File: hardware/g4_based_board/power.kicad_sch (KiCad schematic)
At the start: 13 parts, among them U1 tps2117, U6 AZ1117-3.3

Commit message: auto updated
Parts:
- renumbered C18 to C50, C19 to C51, C22 to C52, D2 to D22, JP20 to JP61, R25 to R70, R77 to R71, R78 to R72, TP4 to TP30, TP5 to TP31, TP6 to TP32, U1 to U6, U6 to U7
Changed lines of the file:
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@@
 		(dnp no)
 		(fields_autoplaced yes)
-		(property "Reference" "#PWR042"
+		(property "Reference" "#PWR0243"
 			(at 192.532 137.922 0)
 			(effects
@@
 			(project "data_logger"
 				(path "/9bc93932-ff5f-4f35-96cf-dfa5f042acb6/ab250e5c-6a0e-43ed-b42b-bd03a881d896"
-					(reference "#PWR042")
+					(reference "#PWR0243")
 					(unit 1)
 				)
@@
 		(dnp no)
 		(fields_autoplaced yes)
-		(property "Reference" "TP6"
+		(property "Reference" "TP32"
 			(at 229.87 124.968 0)
 			(effects
@@
 			(project "data_logger"
 				(path "/9bc93932-ff5f-4f35-96cf-dfa5f042acb6/ab250e5c-6a0e-43ed-b42b-bd03a881d896"
-					(reference "TP6")
+					(reference "TP32")
 					(unit 1)
 				)
@@
 		(dnp no)
 		(fields_autoplaced yes)
-		(property "Reference" "#PWR014"
+		(property "Reference" "#PWR0234"
 			(at 132.08 121.92 0)
 			(effects
@@
 			(project "data_logger"
 				(path "/9bc93932-ff5f-4f35-96cf-dfa5f042acb6/ab250e5c-6a0e-43ed-b42b-bd03a881d896"
-					(reference "#PWR014")
+					(reference "#PWR0234")
 					(unit 1)
 				)
@@
 		(dnp no)
 		(fields_autoplaced yes)
-		(property "Reference" "R25"
+		(property "Reference" "R70"
 			(at 157.226 87.1219 0)
 			(effects
@@
 			(project "data_logger"
 				(path "/9bc93932-ff5f-4f35-96cf-dfa5f042acb6/ab250e5c-6a0e-43ed-b42b-bd03a881d896"
-					(reference "R25")
+					(reference "R70")
 					(unit 1)
 				)
@@
 		(dnp no)
 		(fields_autoplaced yes)
-		(property "Reference" "TP5"
+		(property "Reference" "TP31"
 			(at 195.072 115.57 0)
 			(effects
@@
 			(project "data_logger"
 				(path "/9bc93932-ff5f-4f35-96cf-dfa5f042acb6/ab250e5c-6a0e-43ed-b42b-bd03a881d896"
-					(reference "TP5")
+					(reference "TP31")
 					(unit 1)
 				)
@@
 		(dnp no)
 		(fields_autoplaced yes)
-		(property "Reference" "#PWR0294"
+		(property "Reference" "#PWR0244"
 			(at 204.47 99.822 0)
 			(effects
@@
 			(project "data_logger"
 				(path "/9bc93932-ff5f-4f35-96cf-dfa5f042acb6/ab250e5c-6a0e-43ed-b42b-bd03a881d896"
-					(reference "#PWR0294")
+					(reference "#PWR0244")
 					(unit 1)
 				)
@@
 		(dnp no)
 		(fields_autoplaced yes)
-		(property "Reference" "#PWR0292"
+		(property "Reference" "#PWR0241"
 			(at 177.8 109.982 0)
 			(effects
@@
 			(project "data_logger"
 				(path "/9bc93932-ff5f-4f35-96cf-dfa5f042acb6/ab250e5c-6a0e-43ed-b42b-bd03a881d896"
-					(reference "#PWR0292")
+					(reference "#PWR0241")
 					(unit 1)
 				)
@@
 		(dnp no)
 		(fields_autoplaced yes)
-		(property "Reference" "#PWR091"
+		(property "Reference" "#PWR0247"
 			(at 230.632 123.952 0)
 			(effects
@@
 			(project "data_logger"
 				(path "/9bc93932-ff5f-4f35-96cf-dfa5f042acb6/ab250e5c-6a0e-43ed-b42b-bd03a881d896"
-					(reference "#PWR091")
+					(reference "#PWR0247")
 					(unit 1)
 				)
@@
 		(dnp no)
 		(fields_autoplaced yes)
-		(property "Reference" "TP4"
+		(property "Reference" "TP30"
 			(at 150.622 115.5699 0)
 			(effects
@@
 			(project "data_logger"
 				(path "/9bc93932-ff5f-4f35-96cf-dfa5f042acb6/ab250e5c-6a0e-43ed-b42b-bd03a881d896"
-					(reference "TP4")
+					(reference "TP30")
 					(unit 1)
 				)
@@
 		(dnp no)
 		(fields_autoplaced yes)
-		(property "Reference" "C18"
+		(property "Reference" "C50"
 			(at 161.29 124.333 0)
 			(effects
@@
 			(project "data_logger"
 				(path "/9bc93932-ff5f-4f35-96cf-dfa5f042acb6/ab250e5c-6a0e-43ed-b42b-bd03a881d896"
-					(reference "C18")
+					(reference "C50")
 					(unit 1)
 				)
@@
 		(dnp no)
 		(fields_autoplaced yes)
-		(property "Reference" "R77"
+		(property "Reference" "R71"
 			(at 157.226 92.2019 0)
 			(effects
@@
 			(project "data_logger"
 				(path "/9bc93932-ff5f-4f35-96cf-dfa5f042acb6/ab250e5c-6a0e-43ed-b42b-bd03a881d896"
-					(reference "R77")
+					(reference "R71")
 					(unit 1)
 				)
@@
 		(dnp no)
 		(fields_autoplaced yes)
-		(property "Reference" "#PWR0289"
+		(property "Reference" "#PWR0245"
 			(at 205.74 85.852 0)
 			(effects
@@
 			(project "data_logger"
 				(path "/9bc93932-ff5f-4f35-96cf-dfa5f042acb6/ab250e5c-6a0e-43ed-b42b-bd03a881d896"
-					(reference "#PWR0289")
+					(reference "#PWR0245")
 					(unit 1)
 				)
@@
 		(dnp no)
 		(fields_autoplaced yes)
-		(property "Reference" "#FLG01"
+		(property "Reference" "#FLG028"
 			(at 220.98 118.237 0)
 			(effects
@@
 			(project "data_logger"
 				(path "/9bc93932-ff5f-4f35-96cf-dfa5f042acb6/ab250e5c-6a0e-43ed-b42b-bd03a881d896"
-					(reference "#FLG01")
+					(reference "#FLG028")
 					(unit 1)
 				)
@@
 		(dnp no)
 		(fields_autoplaced yes)
-		(property "Reference" "#PWR040"
+		(property "Reference" "#PWR0239"
 			(at 157.48 137.922 0)
 			(effects
@@
 			(project "data_logger"
 				(path "/9bc93932-ff5f-4f35-96cf-dfa5f042acb6/ab250e5c-6a0e-43ed-b42b-bd03a881d896"
-					(reference "#PWR040")
+					(reference "#PWR0239")
 					(unit 1)
 				)
@@
 		(dnp no)
 		(fields_autoplaced yes)
-		(property "Reference" "#PWR0288"
+		(property "Reference" "#PWR0236"
 			(at 153.162 101.092 0)
 			(effects
@@
 			(project "data_logger"
 				(path "/9bc93932-ff5f-4f35-96cf-dfa5f042acb6/ab250e5c-6a0e-43ed-b42b-bd03a881d896"
-					(reference "#PWR0288")
+					(reference "#PWR0236")
 					(unit 1)
 				)
@@
 		(dnp no)
 		(fields_autoplaced yes)
-		(property "Reference" "#PWR0291"
+		(property "Reference" "#PWR0237"
 			(at 153.67 85.852 0)
 			(effects
@@
 			(project "data_logger"
 				(path "/9bc93932-ff5f-4f35-96cf-dfa5f042acb6/ab250e5c-6a0e-43ed-b42b-bd03a881d896"
-					(reference "#PWR0291")
+					(reference "#PWR0237")
 					(unit 1)
 				)
@@
 		(dnp no)
 		(fields_autoplaced yes)
-		(property "Reference" "JP20"
+		(property "Reference" "JP61"
 			(at 210.82 115.062 0)
 			(effects
@@
 			(project "data_logger"
 				(path "/9bc93932-ff5f-4f35-96cf-dfa5f042acb6/ab250e5c-6a0e-43ed-b42b-bd03a881d896"
-					(reference "JP20")
+					(reference "JP61")
 					(unit 1)
 				)
@@
 		(dnp no)
 		(fields_autoplaced yes)
-		(property "Reference" "U1"
+		(property "Reference" "U6"
 			(at 170.18 80.264 0)
 			(effects
@@
 			(project "data_logger"
 				(path "/9bc93932-ff5f-4f35-96cf-dfa5f042acb6/ab250e5c-6a0e-43ed-b42b-bd03a881d896"
-					(reference "U1")
+					(reference "U6")
 					(unit 1)
 				)
@@
 		(dnp no)
 		(fields_autoplaced yes)
-		(property "Reference" "#PWR026"
+		(property "Reference" "#PWR0235"
 			(at 139.192 135.382 0)
 			(effects
@@
 			(project "data_logger"
 				(path "/9bc93932-ff5f-4f35-96cf-dfa5f042acb6/ab250e5c-6a0e-43ed-b42b-bd03a881d896"
-					(reference "#PWR026")
+					(reference "#PWR0235")
 					(unit 1)
 				)
@@
 		(dnp no)
 		(fields_autoplaced yes)
-		(property "Reference" "R78"
+		(property "Reference" "R72"
 			(at 195.326 88.8999 0)
 			(effects
@@
 			(project "data_logger"
 				(path "/9bc93932-ff5f-4f35-96cf-dfa5f042acb6/ab250e5c-6a0e-43ed-b42b-bd03a881d896"
-					(reference "R78")
+					(reference "R72")
 					(unit 1)
 				)
@@
 		(dnp no)
 		(fields_autoplaced yes)
-		(property "Reference" "#PWR0293"
+		(property "Reference" "#PWR0242"
 			(at 184.912 96.52 0)
 			(effects
@@
 			(project "data_logger"
 				(path "/9bc93932-ff5f-4f35-96cf-dfa5f042acb6/ab250e5c-6a0e-43ed-b42b-bd03a881d896"
-					(reference "#PWR0293")
+					(reference "#PWR0242")
 					(unit 1)
 				)
@@
 		(dnp no)
 		(fields_autoplaced yes)
-		(property "Reference" "#PWR043"
+		(property "Reference" "#PWR0246"
 			(at 227.33 137.16 0)
 			(effects
@@
 			(project "data_logger"
 				(path "/9bc93932-ff5f-4f35-96cf-dfa5f042acb6/ab250e5c-6a0e-43ed-b42b-bd03a881d896"
-					(reference "#PWR043")
+					(reference "#PWR0246")
 					(unit 1)
 				)
@@
 		(on_board yes)
 		(dnp no)
-		(property "Reference" "#PWR0290"
+		(property "Reference" "#PWR0238"
 			(at 154.94 102.362 0)
 			(effects
@@
 			(project "data_logger"
 				(path "/9bc93932-ff5f-4f35-96cf-dfa5f042acb6/ab250e5c-6a0e-43ed-b42b-bd03a881d896"
-					(reference "#PWR0290")
+					(reference "#PWR0238")
 					(unit 1)
 				)
@@
 		(dnp no)
 		(fields_autoplaced yes)
-		(property "Reference" "C19"
+		(property "Reference" "C51"
 			(at 196.342 124.333 0)
 			(effects
@@
 			(project "data_logger"
 				(path "/9bc93932-ff5f-4f35-96cf-dfa5f042acb6/ab250e5c-6a0e-43ed-b42b-bd03a881d896"
-					(reference "C19")
+					(reference "C51")
 					(unit 1)
 				)
@@
 		(dnp no)
 		(fields_autoplaced yes)
-		(property "Reference" "C22"
+		(property "Reference" "C52"
 			(at 207.518 88.3919 0)
 			(effects
@@
 			(project "data_logger"
 				(path "/9bc93932-ff5f-4f35-96cf-dfa5f042acb6/ab250e5c-6a0e-43ed-b42b-bd03a881d896"
-					(reference "C22")
+					(reference "C52")
 					(unit 1)
 				)
@@
 		(on_board yes)
 		(dnp no)
-		(property "Reference" "U6"
+		(property "Reference" "U7"
 			(at 173.482 115.062 0)
 			(effects
@@
 			(project "data_logger"
 				(path "/9bc93932-ff5f-4f35-96cf-dfa5f042acb6/ab250e5c-6a0e-43ed-b42b-bd03a881d896"
-					(reference "U6")
+					(reference "U7")
 					(unit 1)
 				)
@@
 		(dnp no)
 		(fields_autoplaced yes)
-		(property "Reference" "#PWR041"
+		(property "Reference" "#PWR0240"
 			(at 173.482 137.922 0)
 			(effects
@@
 			(project "data_logger"
 				(path "/9bc93932-ff5f-4f35-96cf-dfa5f042acb6/ab250e5c-6a0e-43ed-b42b-bd03a881d896"
-					(reference "#PWR041")
+					(reference "#PWR0240")
 					(unit 1)
 				)
@@
 		(on_board yes)
 		(dnp no)
-		(property "Reference" "D2"
+		(property "Reference" "D22"
 			(at 133.477 125.222 90)
 			(effects
@@
 			(project "data_logger"
 				(path "/9bc93932-ff5f-4f35-96cf-dfa5f042acb6/ab250e5c-6a0e-43ed-b42b-bd03a881d896"
-					(reference "D2")
-					(unit 1)
-				)
+					(reference "D22")
+					(unit 1)
+				)

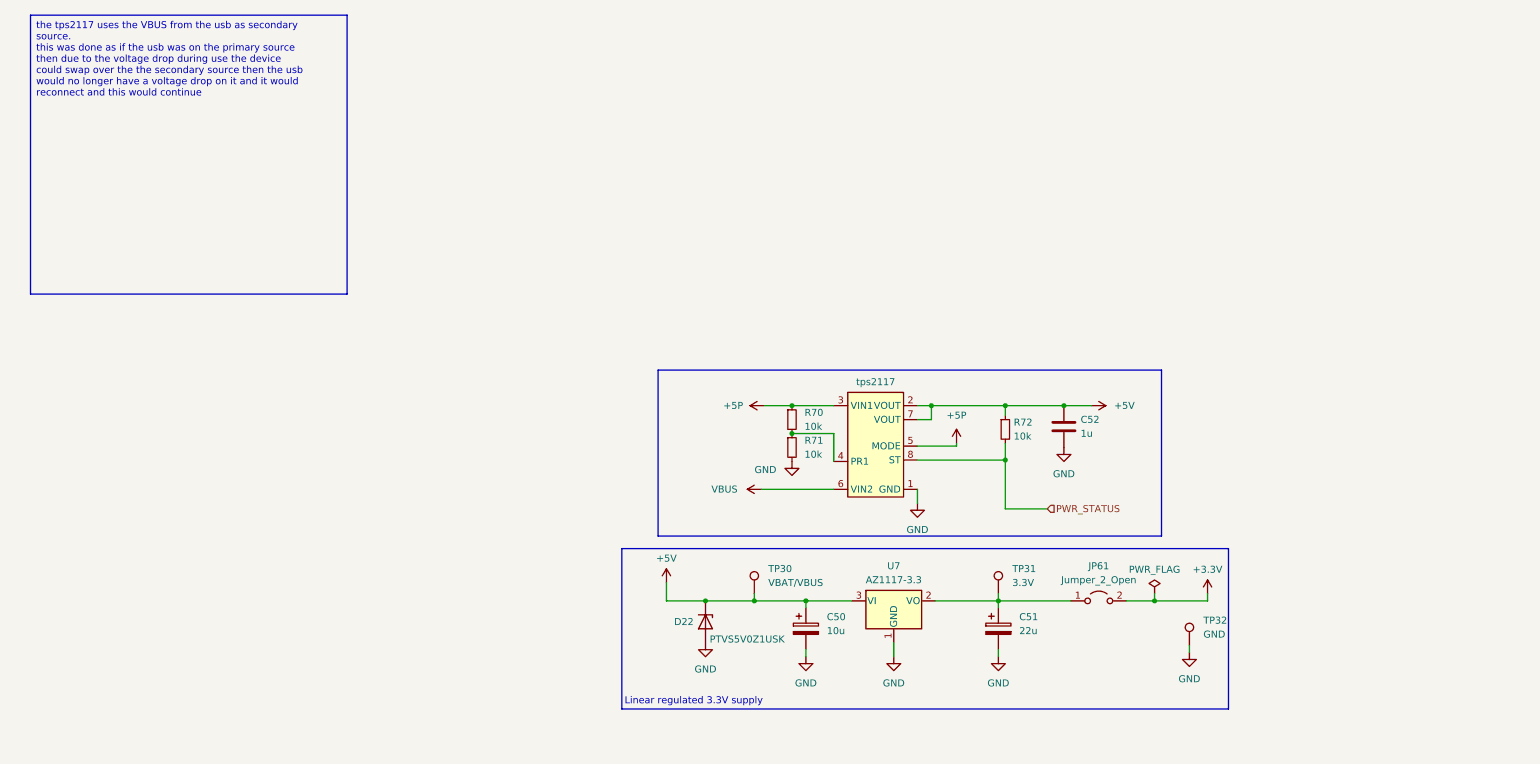
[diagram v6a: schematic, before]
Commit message: added bulk decoupling and status leds
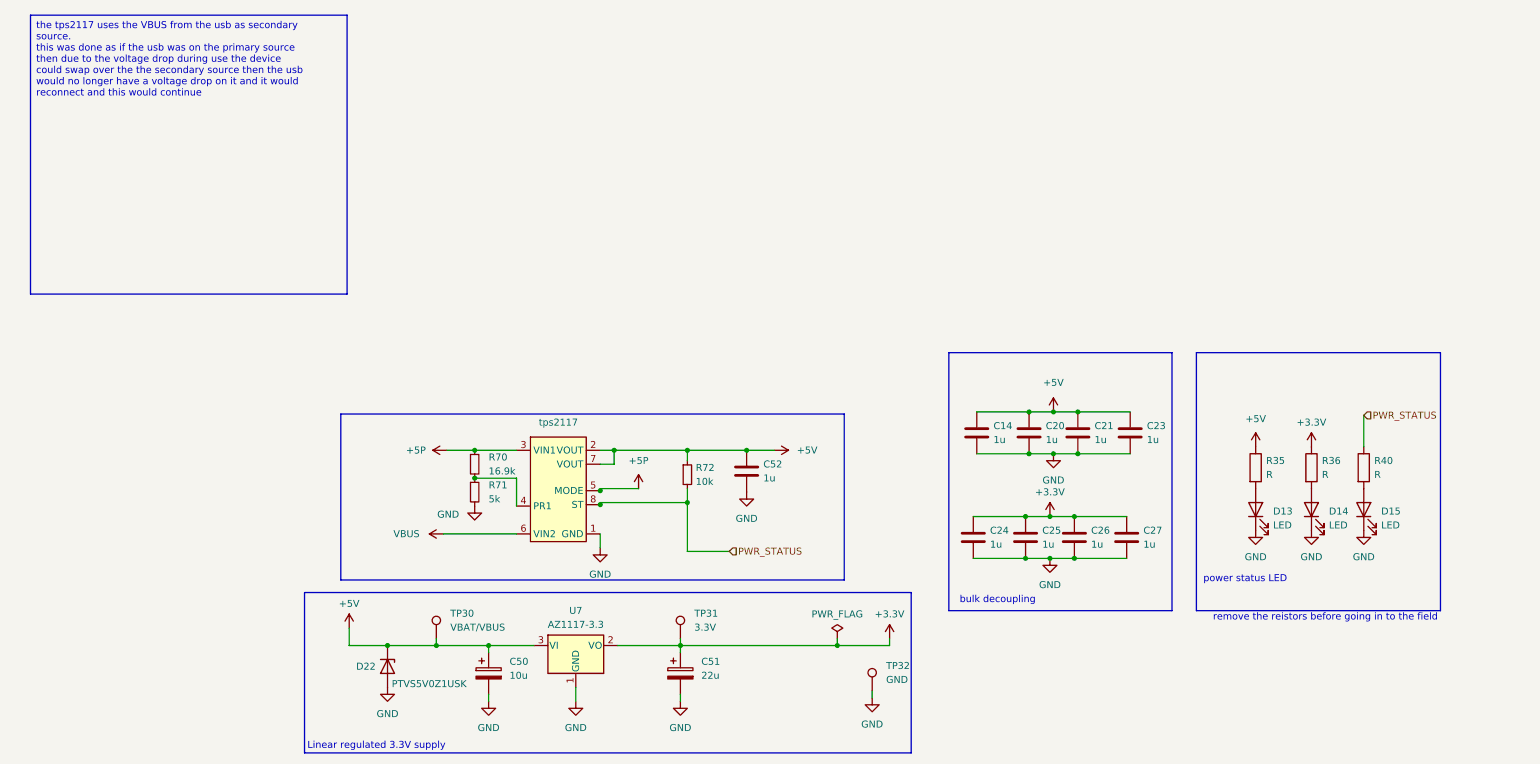
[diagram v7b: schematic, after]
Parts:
- removed JP61: Jumper_2_Open, Jumper:SolderJumper-2_P1.3mm_Open_TrianglePad1.0x1.5mm, symbol Jumper:Jumper_2_Open
- added C14, C20, C21, C23, C24, C25, C26, C27: 1u, Capacitor_SMD:C_0603_1608Metric_Pad1.08x0.95mm_HandSolder, symbol Device:C
- added D13, D14, D15: LED, LED_SMD:LED_0603_1608Metric, symbol Device:LED
- added R35, R36, R40: R, Resistor_SMD:R_0603_1608Metric_Pad0.98x0.95mm_HandSolder, symbol Device:R
- R70: value 10k -> 16.9k
- R71: value 10k -> 5k
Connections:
- net +3.3V: now also C51.1, TP31.1, U7.2 (VO), C24.1, C25.1, C26.1, C27.1, R36.1
- net +5V: now also C14.1, C20.1, C21.1, C23.1, R35.1
- net GND: now also C14.2, C20.2, C21.2, C23.2, C24.2, C25.2, C26.2, C27.2, D13.1 (K), D14.1 (K), D15.1 (K)
- net PWR_STATUS: now also R40.1
- new net: D15.2 (A), R40.2
- new net: D14.2 (A), R36.2
- new net: D13.2 (A), R35.2
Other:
- note added: "bulk decoupling"
- note added: "power status LED"
- note added: "remove the reistors before going in to the field"
- moved on the sheet: C50, C51, C52, D22, R70, R71, R72, TP30, TP31, TP32, U7
